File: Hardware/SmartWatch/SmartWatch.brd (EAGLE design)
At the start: 100 x 80 mm, 1 part

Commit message: adding things to library
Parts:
- added U2: (no value), SmartWatch:BLE_MODULE_RAYTAC_MDBT40
- U1: value (none) -> STM32L476; device SmartWatch:BLE_MODULE_RAYTAC_MDBT40 -> SmartWatch:TQFP64-10X10
- moved U1 44.9 mm to (-7.62, 7.62)
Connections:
- net AVDD: now also U2.3; no longer U1.3
- net DCC: now also U2.15; no longer U1.15
- net DEC2: now also U2.41; no longer U1.41
- net GND: now also U2.1, U2.13, U2.2, U2.25, U2.42; no longer U1.1, U1.13, U1.2, U1.25, U1.42
- net VDD: now also U2.14; no longer U1.14
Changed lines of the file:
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@@
 </autorouter>
 <elements>
-<element name="U1" library="SmartWatch" package="BLE_MODULE_RAYTAC_MDBT40" value="" x="11.43" y="48.26"/>
+<element name="U2" library="SmartWatch" package="BLE_MODULE_RAYTAC_MDBT40" value="" x="11.43" y="48.26"/>
+<element name="U1" library="SmartWatch" package="TQFP64-10X10" value="STM32L476" x="-7.62" y="7.62"/>
 </elements>
 <signals>
 <signal name="AVDD">
-<contactref element="U1" pad="3"/>
+<contactref element="U2" pad="3"/>
 </signal>
 <signal name="DCC">
-<contactref element="U1" pad="15"/>
+<contactref element="U2" pad="15"/>
 </signal>
 <signal name="DEC2">
-<contactref element="U1" pad="41"/>
+<contactref element="U2" pad="41"/>
 </signal>
 <signal name="GND">
-<contactref element="U1" pad="1"/>
-<contactref element="U1" pad="2"/>
-<contactref element="U1" pad="13"/>
-<contactref element="U1" pad="25"/>
-<contactref element="U1" pad="42"/>
+<contactref element="U2" pad="1"/>
+<contactref element="U2" pad="2"/>
+<contactref element="U2" pad="13"/>
+<contactref element="U2" pad="25"/>
+<contactref element="U2" pad="42"/>
 <wire x1="15.63" y1="39.435" x2="7.23" y2="39.435" width="0" layer="19" extent="1-1"/>
 <wire x1="6.605" y1="51.56" x2="7.23" y2="39.435" width="0" layer="19" extent="1-1"/>
@@
 </signal>
 <signal name="VDD">
-<contactref element="U1" pad="14"/>
+<contactref element="U2" pad="14"/>
 </signal>
 </signals>

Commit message: Continued work on schematic and libraries
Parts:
- added C1, C14, C3: 1uF, microbuilder:0603-MINI
- added C10: 1.0uF, microbuilder:0603-MINI
- added C11, C4, C5, C8: 0.1uF, microbuilder:0603-MINI
- added C12: 47uF, resistor:C1206
- added C2, C6: 10uF/16V, microbuilder:0603-MINI
- added C7, C9: 10uF, microbuilder:0603-MINI
- added D1, D3: 1N4148, microbuilder:SOD-323
- added D2: BAT54T1G, microbuilder:SOD-123
- added L1: 10uH, microbuilder:INDUCTOR_1007
- added R1, R10, R11, R12, R2: 10k, resistor:R0603
- added R3, R8: 4.7k, resistor:R0603
- added R4: 600K, resistor:R0603
- added R5: 50, resistor:R0603
- added R6: 100K, resistor:R0603
- added R7, R9: 10K, resistor:R0603
- added U$27: LTC3557, SmartWatch:28QFN4X4
- added U$5: BNO055, SmartWatch:LGA28
- added U3: UG-2828GDEDF11, microbuilder:FPC_XF2M-3015-1A
- added U4: FAN5331SX, microbuilder:SOT23-5@1
- added U5: APDS-9960, SparkFun-Sensors:APDS-9960
- moved U2 28.1 mm to (30.6, 27.7)
- moved U1 26.5 mm to (17.8, 15.2), flipped to the bottom, turned to 90 degrees
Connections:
- removed net AVDD: U2.3
- removed net VDD: U2.14
- new net +3V3: C1.2, R1.2, U2.14, U2.3
- new net 13V: C2.2, C8.1, D2.C, R6.2, U3.P$29
- new net 3.3V: C10.2, C11.2, C12.1, C3.2, C5.2, C7.1, C9.2, L1.P$1, R3.2, R8.2, R9.2, U$5.28, U$5.3, U$5.4, U3.P$27, U3.P$4, U4.4, U4.5, U5.5, U5.8
- new net BT_CS: R1.1, U2.7
- new net BT_IRQ: U2.8
- new net BT_MISO: U2.5
- new net BT_MOSI: U2.6
- new net BT_SCK: U2.4
- new net G_INT: R9.1, U5.2
- new net IMU_INT: U$5.14
- new net IMU_NRESET: U$5.11
- new net MOSI/DATA1: U3.P$18
- new net N$1: R4.2, U3.P$9
- new net N$11: D1.C, D3.A
- new net N$13: R12.2, U$5.5
- new net N$14: R11.2, U$5.6
- new net N$2: C14.2, U3.P$5
- new net N$3: R10.1, U$5.17
- new net N$4: C4.2, U$5.9
- new net N$5: D2.A, L1.P$2, U4.1
- new net N$6: R5.2, U3.P$26
- new net N$7: D1.A, R5.1
- new net N$8: C8.2, R6.1, R7.2, U4.3
- new net N$9: U5.3, U5.4
- new net OLED_BS0: R2.2, U3.P$14
- new net OLED_CS: U3.P$12
- new net OLED_DC: U3.P$11
- new net OLED_RES: U3.P$10
- new net SCK/DATA0: U3.P$17
- new net SCL: R3.1, U$5.19, U5.7
- new net SDA: R8.1, U$5.20, U5.1
- new net VCOMH1: C6.1, U3.P$28
- net GND: now also C1.1, C10.1, C11.1, C12.2, C14.1, C2.1, C3.1, C4.1, C5.1, C6.2, C7.2, C9.1, D3.C, R10.2, R11.1, R12.1, R2.1, R4.1, R7.1, U$5.10, U$5.15, U$5.16, U$5.18, U$5.2, U$5.25, U2.16, U3.P$1, U3.P$13, U3.P$3, U3.P$30, U4.2, U5.6
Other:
- board size 100 x 80 mm -> 36.8 x 36.8 mm

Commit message: renamed part
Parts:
- renumbered U$27 to U6
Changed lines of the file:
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@@
 <element name="C12" library="resistor" package="C1206" value="47uF" x="5.08" y="2.54"/>
 <element name="C1" library="microbuilder" package="0603-MINI" value="1uF" x="33.02" y="11.43" rot="R90"/>
-<element name="U$27" library="SmartWatch" package="28QFN4X4" value="LTC3557" x="17.78" y="15.24"/>
+<element name="U6" library="SmartWatch" package="28QFN4X4" value="LTC3557" x="17.78" y="15.24"/>
 </elements>
 <signals>

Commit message: Updated schematic
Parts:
- added JP1: (no value), SparkFun-Connectors:USB-B-MICRO-SMD_V03
- added RN1: (no value), MicroBoard:EXBV4V
- moved C12 59.5 mm to (43.2, 48.3), turned to 270 degrees
- moved R2 55.7 mm to (45.7, 48.3), turned to 270 degrees
- moved R5 54.8 mm to (47.0, 48.3), turned to 270 degrees
- moved D2 45.9 mm to (38.1, 48.3), turned to 90 degrees
- moved C1 40.4 mm to (49.5, 48.3)
- moved C3 39.4 mm to (2.54, 45.7), turned to 270 degrees
- moved L1 37.7 mm to (34.3, 45.7), turned to 90 degrees
- moved R4 36.9 mm to (5.08, 45.7), turned to 270 degrees
- moved C2 34.7 mm to (7.62, 45.7), turned to 270 degrees
- moved C6 32.7 mm to (10.2, 45.7), turned to 270 degrees
- moved C8 31.0 mm to (33.0, 49.5), turned to 90 degrees
- moved D3 30.9 mm to (12.7, 45.7), turned to 270 degrees
- moved R6 30.3 mm to (27.9, 49.5), turned to 90 degrees
- moved C4 30.2 mm to (30.5, 45.7), turned to 270 degrees
- moved D1 29.5 mm to (15.2, 45.7), turned to 270 degrees
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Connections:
- new net D+: RN1.4
- new net D-: RN1.3
- new net N$10: JP1.D+1, RN1.1
- new net N$15: JP1.D-1, RN1.2
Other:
- board size 36.8 x 36.8 mm -> 36.8 x 40.6 mm

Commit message: added to schematic more
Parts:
- added U$16, U$28, U$29, U$30, U$31, U$32: PTS840-GM, SmartWatch:PTS840-GM
- U3: device microbuilder:FPC_XF2M-3015-1A -> SmartWatch:FPC_XF2M-3015-1A
- U4: device microbuilder:SOT23-5@1 -> SmartWatch:SOT23-5$1
- moved JP1 3.50 mm to (1.91, 24.2)
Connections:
- net 13V: now also U3.P$2; no longer U3.P$29
- net GND: now also U3.P$18, U3.P$28; no longer U3.P$13, U3.P$3
- net MOSI/DATA1: now also U3.P$13; no longer U3.P$18
- net N$1: now also U3.P$22; no longer U3.P$9
- net N$2: now also U3.P$26; no longer U3.P$5
- net N$6: now also U3.P$5; no longer U3.P$26
- net OLED_BS0: now also U3.P$17; no longer U3.P$14
- net OLED_CS: now also U3.P$19; no longer U3.P$12
- net OLED_DC: now also U3.P$20; no longer U3.P$11
- net OLED_RES: now also U3.P$21; no longer U3.P$10
- net SCK/DATA0: now also U3.P$14; no longer U3.P$17
- net VCOMH1: now also U3.P$3; no longer U3.P$28
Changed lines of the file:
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@@
 <setting verticaltext="up"/>
 </settings>
-<grid distance="0.05" unitdist="inch" unit="inch" style="lines" multiple="1" display="yes" altdistance="0.005" altunitdist="inch" altunit="inch"/>
+<grid distance="1" unitdist="mm" unit="mm" style="lines" multiple="1" display="yes" altdistance="0.1" altunitdist="mm" altunit="mm"/>
 <layers>
 <layer number="1" name="Top" color="4" fill="1" visible="yes" active="yes"/>
@@
 <layer number="46" name="Milling" color="3" fill="1" visible="no" active="yes"/>
 <layer number="47" name="Measures" color="7" fill="1" visible="no" active="yes"/>
-<layer number="48" name="Document" color="7" fill="1" visible="no" active="yes"/>
-<layer number="49" name="Reference" color="7" fill="1" visible="no" active="yes"/>
+<layer number="48" name="Document" color="7" fill="1" visible="yes" active="yes"/>
+<layer number="49" name="Reference" color="7" fill="1" visible="yes" active="yes"/>
 <layer number="50" name="dxf" color="7" fill="1" visible="no" active="no"/>
 <layer number="51" name="tDocu" color="6" fill="1" visible="yes" active="yes"/>
@@
 <wire x1="36.83" y1="40.64" x2="0" y2="40.64" width="0" layer="20"/>
 <wire x1="0" y1="40.64" x2="0" y2="0" width="0" layer="20"/>
+<rectangle x1="1" y1="6" x2="36" y2="31" layer="49" rot="R90"/>
 </plain>
 <attributes>
@@
 <element name="R5" library="resistor" package="R0603" value="50" x="46.99" y="48.26" rot="R270"/>
 <element name="D1" library="microbuilder" package="SOD-323" value="1N4148" x="15.24" y="45.72" rot="R270"/>
-<element name="U3" library="microbuilder" package="FPC_XF2M-3015-1A" value="UG-2828GDEDF11" x="19.05" y="6.35" rot="MR180"/>
+<element name="U3" library="SmartWatch" package="FPC_XF2M-3015-1A" value="UG-2828GDEDF11" x="19.05" y="6.35" rot="MR180"/>
 <element name="C6" library="microbuilder" package="0603-MINI" value="10uF/16V" x="10.16" y="45.72" rot="R270"/>
 <element name="D3" library="microbuilder" package="SOD-323" value="1N4148" x="12.7" y="45.72" rot="R270"/>
 <element name="R2" library="resistor" package="R0603" value="10k" x="45.72" y="48.26" rot="R270"/>
-<element name="U4" library="microbuilder" package="SOT23-5@1" value="FAN5331SX" x="13.97" y="50.8"/>
+<element name="U4" library="SmartWatch" package="SOT23-5$1" value="FAN5331SX" x="13.97" y="50.8"/>
 <element name="C7" library="microbuilder" package="0603-MINI" value="10uF" x="30.48" y="49.53" rot="R90"/>
 <element name="L1" library="microbuilder" package="INDUCTOR_1007" value="10uH" x="34.29" y="45.72" rot="R90"/>
@@
 <element name="C1" library="microbuilder" package="0603-MINI" value="1uF" x="49.53" y="48.26" rot="R90"/>
 <element name="U6" library="SmartWatch" package="28QFN4X4" value="LTC3557" x="10.16" y="13.97"/>
-<element name="JP1" library="SparkFun-Connectors" package="USB-B-MICRO-SMD_V03" value="" x="1.905" y="27.686">
-<attribute name="PROD_ID" value="CONN-11752" x="1.905" y="27.686" size="1.778" layer="27" font="vector" ratio="15" display="off"/>
+<element name="JP1" library="SparkFun-Connectors" package="USB-B-MICRO-SMD_V03" value="" x="1.905" y="24.186">
+<attribute name="PROD_ID" value="CONN-11752" x="1.905" y="24.186" size="1.778" layer="27" font="vector" ratio="15" display="off"/>
 </element>
 <element name="RN1" library="MicroBoard" package="EXBV4V" value="" x="7.62" y="27.94" rot="R90">
@@
 <attribute name="DIGIKEY" value="RHM1381CT-ND" x="7.62" y="27.94" size="1.778" layer="27" font="vector" ratio="15" rot="R90" display="off"/>
 </element>
+<element name="U$16" library="SmartWatch" package="PTS840-GM" value="PTS840-GM" x="1.5" y="6" rot="R270"/>
+<element name="U$28" library="SmartWatch" package="PTS840-GM" value="PTS840-GM" x="1.5" y="13.5" rot="R270"/>
+<element name="U$29" library="SmartWatch" package="PTS840-GM" value="PTS840-GM" x="1.5" y="35" rot="R270"/>
+<element name="U$30" library="SmartWatch" package="PTS840-GM" value="PTS840-GM" x="35.4" y="6.5" rot="R90"/>
+<element name="U$31" library="SmartWatch" package="PTS840-GM" value="PTS840-GM" x="35.4" y="36" rot="R90"/>
+<element name="U$32" library="SmartWatch" package="PTS840-GM" value="PTS840-GM" x="35.4" y="21.5" rot="R90"/>
 </elements>
 <signals>
@@
 <contactref element="U2" pad="16"/>
 <contactref element="R4" pad="1"/>
-<contactref element="U3" pad="P$3"/>
-<contactref element="U3" pad="P$13"/>
+<contactref element="U3" pad="P$28"/>
+<contactref element="U3" pad="P$18"/>
 <contactref element="C7" pad="2"/>
 <contactref element="R7" pad="1"/>
 <contactref element="U4" pad="2"/>
-<contactref element="U3" pad="P$1"/>
+<contactref element="U3" pad="P$30"/>
 <contactref element="R2" pad="1"/>
 <contactref element="D3" pad="C"/>
 <contactref element="C6" pad="2"/>
 <contactref element="C2" pad="1"/>
-<contactref element="U3" pad="P$30"/>
+<contactref element="U3" pad="P$1"/>
 <contactref element="C3" pad="1"/>
 <contactref element="U$5" pad="2"/>
@@
 <wire x1="23.427" y1="22.671" x2="21.327" y2="22.671" width="0" layer="19" extent="1-1"/>
 <wire x1="29.727" y1="22.671" x2="23.427" y2="22.671" width="0" layer="19" extent="1-1"/>
-<wire x1="20.3" y1="8.98" x2="21.327" y2="22.671" width="0" layer="19" extent="1-16"/>
-<wire x1="25.3" y1="8.98" x2="20.3" y2="8.98" width="0" layer="19" extent="16-16"/>
-<wire x1="26.3" y1="8.98" x2="25.3" y2="8.98" width="0" layer="19" extent="16-16"/>
-<wire x1="11.8" y1="8.98" x2="20.3" y2="8.98" width="0" layer="19" extent="16-16"/>
+<wire x1="26.3" y1="8.98" x2="23.427" y2="22.671" width="0" layer="19" extent="1-16"/>
+<wire x1="17.8" y1="8.98" x2="26.3" y2="8.98" width="0" layer="19" extent="16-16"/>
+<wire x1="12.8" y1="8.98" x2="17.8" y2="8.98" width="0" layer="19" extent="16-16"/>
+<wire x1="11.8" y1="8.98" x2="12.8" y2="8.98" width="0" layer="19" extent="16-16"/>
 </signal>
 <signal name="+3V3">
@@
 </signal>
 <signal name="OLED_BS0">
+<contactref element="U3" pad="P$17"/>
+<contactref element="R2" pad="2"/>
+<wire x1="18.3" y1="8.98" x2="45.72" y2="47.41" width="0" layer="19" extent="1-16"/>
+</signal>
+<signal name="MOSI/DATA1">
+<contactref element="U3" pad="P$13"/>
+</signal>
+<signal name="SCK/DATA0">
 <contactref element="U3" pad="P$14"/>
-<contactref element="R2" pad="2"/>
-<wire x1="19.8" y1="8.98" x2="45.72" y2="47.41" width="0" layer="19" extent="1-16"/>
-</signal>
-<signal name="MOSI/DATA1">
-<contactref element="U3" pad="P$18"/>
-</signal>
-<signal name="SCK/DATA0">
-<contactref element="U3" pad="P$17"/>
 </signal>
 <signal name="OLED_CS">
-<contactref element="U3" pad="P$12"/>
+<contactref element="U3" pad="P$19"/>
 </signal>
 <signal name="OLED_DC">
-<contactref element="U3" pad="P$11"/>
+<contactref element="U3" pad="P$20"/>
 </signal>
 <signal name="OLED_RES">
-<contactref element="U3" pad="P$10"/>
+<contactref element="U3" pad="P$21"/>
 </signal>
 <signal name="VCOMH1">
-<contactref element="U3" pad="P$28"/>
+<contactref element="U3" pad="P$3"/>
 <contactref element="C6" pad="1"/>
-<wire x1="12.8" y1="8.98" x2="10.16" y2="46.47" width="0" layer="19" extent="1-16"/>
+<wire x1="25.3" y1="8.98" x2="10.16" y2="46.47" width="0" layer="19" extent="1-16"/>
 </signal>
 <signal name="N$6">
 <contactref element="R5" pad="2"/>
-<contactref element="U3" pad="P$26"/>
-<wire x1="13.8" y1="8.98" x2="46.99" y2="47.41" width="0" layer="19" extent="1-16"/>
+<contactref element="U3" pad="P$5"/>
+<wire x1="24.3" y1="8.98" x2="46.99" y2="47.41" width="0" layer="19" extent="1-16"/>
 </signal>
 <signal name="N$7">
@@
 </signal>
 <signal name="3.3V">
+<contactref element="U3" pad="P$27"/>
+<contactref element="C3" pad="2"/>
 <contactref element="U3" pad="P$4"/>
-<contactref element="C3" pad="2"/>
-<contactref element="U3" pad="P$27"/>
 <contactref element="C7" pad="1"/>
 <contactref element="U4" pad="5"/>
@@
 <signal name="13V">
 <contactref element="C2" pad="2"/>
-<contactref element="U3" pad="P$29"/>
+<contactref element="U3" pad="P$2"/>
 <contactref element="C8" pad="1"/>
+<contactref element="D2" pad="C"/>
 <contactref element="R6" pad="2"/>
-<contactref element="D2" pad="C"/>
 <wire x1="33.02" y1="48.78" x2="38.1" y2="46.41" width="0" layer="19" extent="1-1"/>
 <wire x1="27.94" y1="50.38" x2="33.02" y2="48.78" width="0" layer="19" extent="1-1"/>
 <wire x1="7.62" y1="44.97" x2="27.94" y2="50.38" width="0" layer="19" extent="1-1"/>
-<wire x1="12.3" y1="8.98" x2="7.62" y2="44.97" width="0" layer="19" extent="1-16"/>
+<wire x1="25.8" y1="8.98" x2="38.1" y2="46.41" width="0" layer="19" extent="1-16"/>
 </signal>
 <signal name="N$11">
@@
 <signal name="N$1">
 <contactref element="R4" pad="2"/>
-<contactref element="U3" pad="P$9"/>
-<wire x1="22.3" y1="8.98" x2="5.08" y2="44.87" width="0" layer="19" extent="1-16"/>
+<contactref element="U3" pad="P$22"/>
+<wire x1="15.8" y1="8.98" x2="5.08" y2="44.87" width="0" layer="19" extent="1-16"/>
 </signal>
 <signal name="N$2">
-<contactref element="U3" pad="P$5"/>
+<contactref element="U3" pad="P$26"/>
 <contactref element="C14" pad="2"/>
-<wire x1="24.3" y1="8.98" x2="22.86" y2="44.97" width="0" layer="19" extent="1-16"/>
+<wire x1="13.8" y1="8.98" x2="22.86" y2="44.97" width="0" layer="19" extent="1-16"/>
 </signal>
 <signal name="N$4">
@@
 <contactref element="JP1" pad="D+1"/>
 <contactref element="RN1" pad="1"/>
-<wire x1="4.63" y1="27.686" x2="8.395" y2="27.54" width="0" layer="19" extent="1-1"/>
+<wire x1="4.63" y1="24.186" x2="8.395" y2="27.54" width="0" layer="19" extent="1-1"/>
 </signal>
 <signal name="N$15">
 <contactref element="JP1" pad="D-1"/>
 <contactref element="RN1" pad="2"/>
-<wire x1="4.63" y1="28.336" x2="8.395" y2="28.34" width="0" layer="19" extent="1-1"/>
+<wire x1="4.63" y1="24.836" x2="8.395" y2="28.34" width="0" layer="19" extent="1-1"/>
 </signal>
 <signal name="D+">

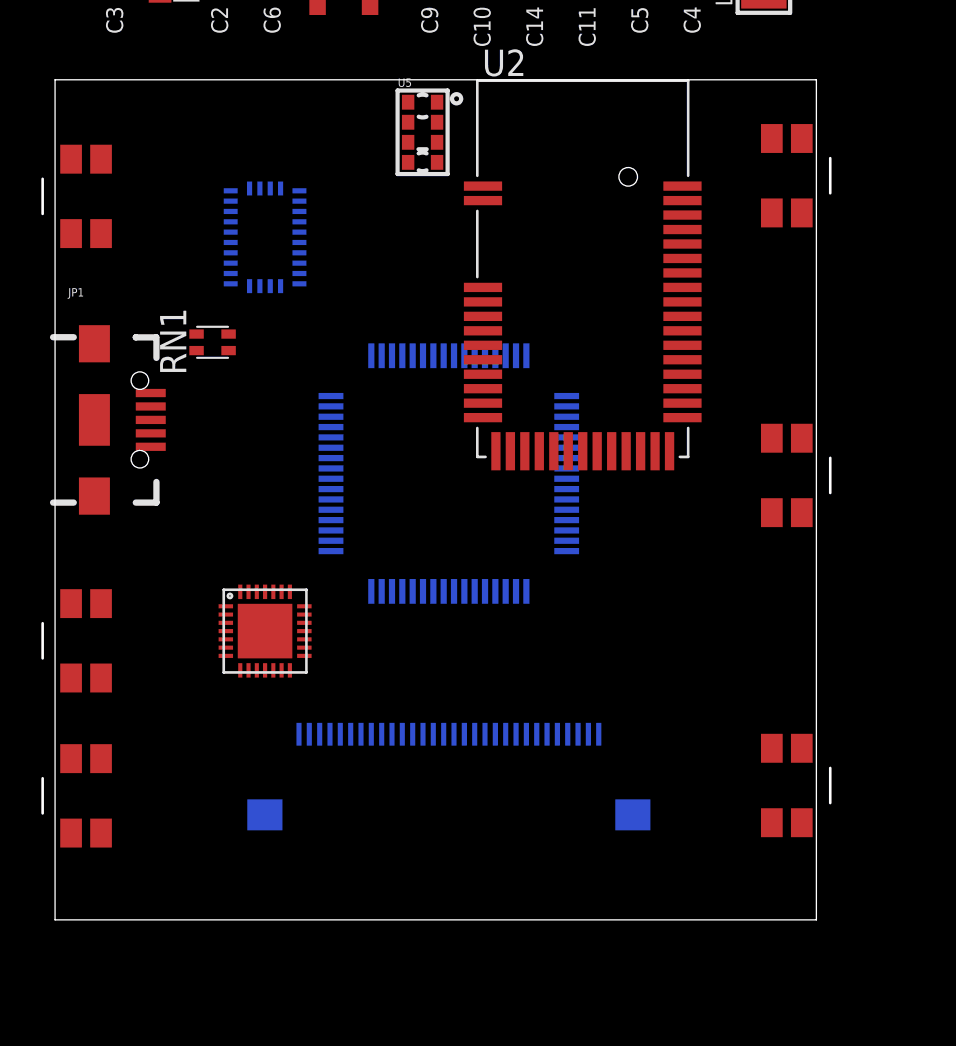
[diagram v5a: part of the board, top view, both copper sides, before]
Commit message: created usb part
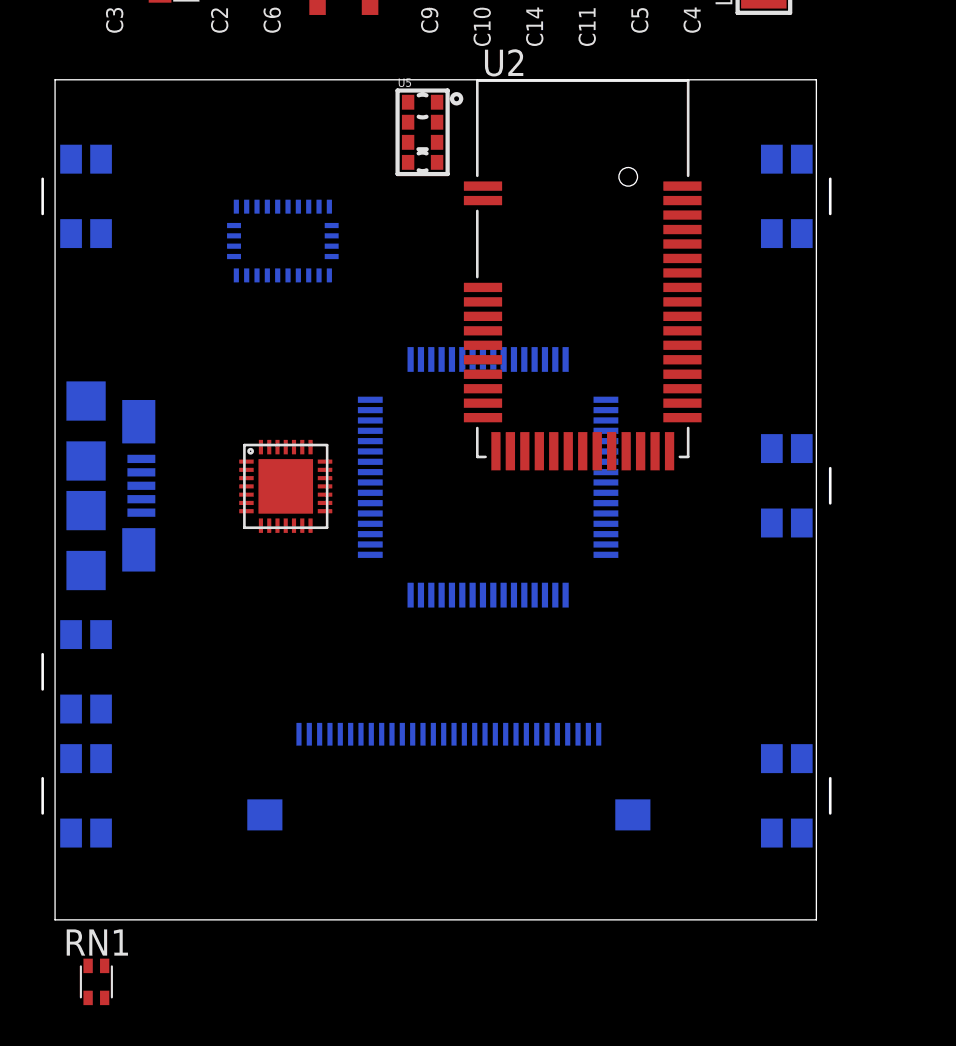
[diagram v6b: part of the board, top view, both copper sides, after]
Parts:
- removed JP1: (no value), SparkFun-Connectors:USB-B-MICRO-SMD_V03
- removed U$28, U$30, U$31, U$32: PTS840-GM, SmartWatch:PTS840-GM
- added BTN_BOOT0, BTN_DN, BTN_NRST, BTN_SEL, BTN_UP: PTS840-GM, SmartWatch:PTS840-GM
- U$16: value PTS840-GM -> MICRO-USB; device SmartWatch:PTS840-GM -> SmartWatch:MICRO-USB
- moved RN1 31.4 mm to (2.00, -3.00), turned to 0 degrees
- moved U$16 15.0 mm to (1.50, 21.0), flipped to the bottom, turned to 90 degrees
- moved U6 7.07 mm to (11.2, 21.0)
- moved U1 1.91 mm to (20.9, 21.4), turned to 270 degrees
- moved U$5 0.88 mm to (11.0, 32.8), turned to 180 degrees
- flipped BTN_BACK to the bottom, turned to 90 degrees
- renumbered U$29 to BTN_BACK
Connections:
- removed net N$10: JP1.D+1, RN1.1
- new net ID: RN1.3, U$16.3
- new net N$17: U$16.4
- new net VUSB: U$16.1
- net D+: now also RN1.2; no longer RN1.4
- net D-: now also RN1.1; no longer RN1.3
- net GND: now also U$16.10, U$16.11, U$16.5, U$16.6, U$16.7, U$16.8, U$16.9
- net N$15: now also RN1.4, U$16.2; no longer JP1.D-1, RN1.2

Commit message: hardware updates
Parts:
- added C13, C15: 10uF, microbuilder:0603-MINI
- added C16, C17: 2.2uF, microbuilder:0603-MINI
- added R13, R14, R15, R16, R17, R18: 10K, resistor:R0603
- added R19: 2.5k, resistor:R0603
- moved RN1 24.5 mm to (7.00, 21.0), flipped to the bottom, turned to 270 degrees
- moved U6 1.00 mm to (11.1, 22.0)
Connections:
- new net BNT_NRST: BTN_NRST.1, BTN_NRST.2, R13.2
- new net BTN_BACK: BTN_BACK.1, BTN_BACK.2, R15.2
- new net BTN_BOOT0: BTN_BOOT0.1, BTN_BOOT0.2, R14.2
- new net BTN_DN: BTN_DN.1, BTN_DN.2, R16.2
- new net BTN_SEL: BTN_SEL.1, BTN_SEL.2, R18.2
- new net BTN_UP: BTN_UP.1, BTN_UP.2, R17.2
- new net CHRG: U6.28
- new net N$10: RN1.3, U$16.2
- new net N$16: R19.2, U6.20
- new net N$19: C17.1, U6.6
- new net N$20: C16.1, U6.16
- new net VBAT: U6.22
- new net VOUT: C15.2, U6.23
- net 3.3V: now also BTN_BACK.3, BTN_BACK.4, BTN_BOOT0.3, BTN_BOOT0.4, BTN_DN.3, BTN_DN.4, BTN_NRST.3, BTN_NRST.4, BTN_SEL.3, BTN_SEL.4, BTN_UP.3, BTN_UP.4
- net D+: now also RN1.1; no longer RN1.2
- net D-: now also RN1.2; no longer RN1.1
- net GND: now also C13.1, C15.1, C16.2, C17.2, R13.1, R14.1, R15.1, R16.1, R17.1, R18.1, R19.1, U6.19, U6.29
- net ID: now also RN1.4; no longer RN1.3
- net N$15: now also C13.2, U6.24; no longer RN1.4, U$16.2
